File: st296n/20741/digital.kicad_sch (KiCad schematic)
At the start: 61 parts, among them J2 ID, Q14 "1A", U1 8051, U13 74LS155, U2 74LS573, U21 74LS174, U22 74LS174, U23 74LS174, U24 74LS257, U27 74LS00, U28 74LS196, U29 74LS123, U3 74LS14, U30 74F08, U4 CDM6264, U9 11741-502, Y1 10MHz, Y2 20MHz

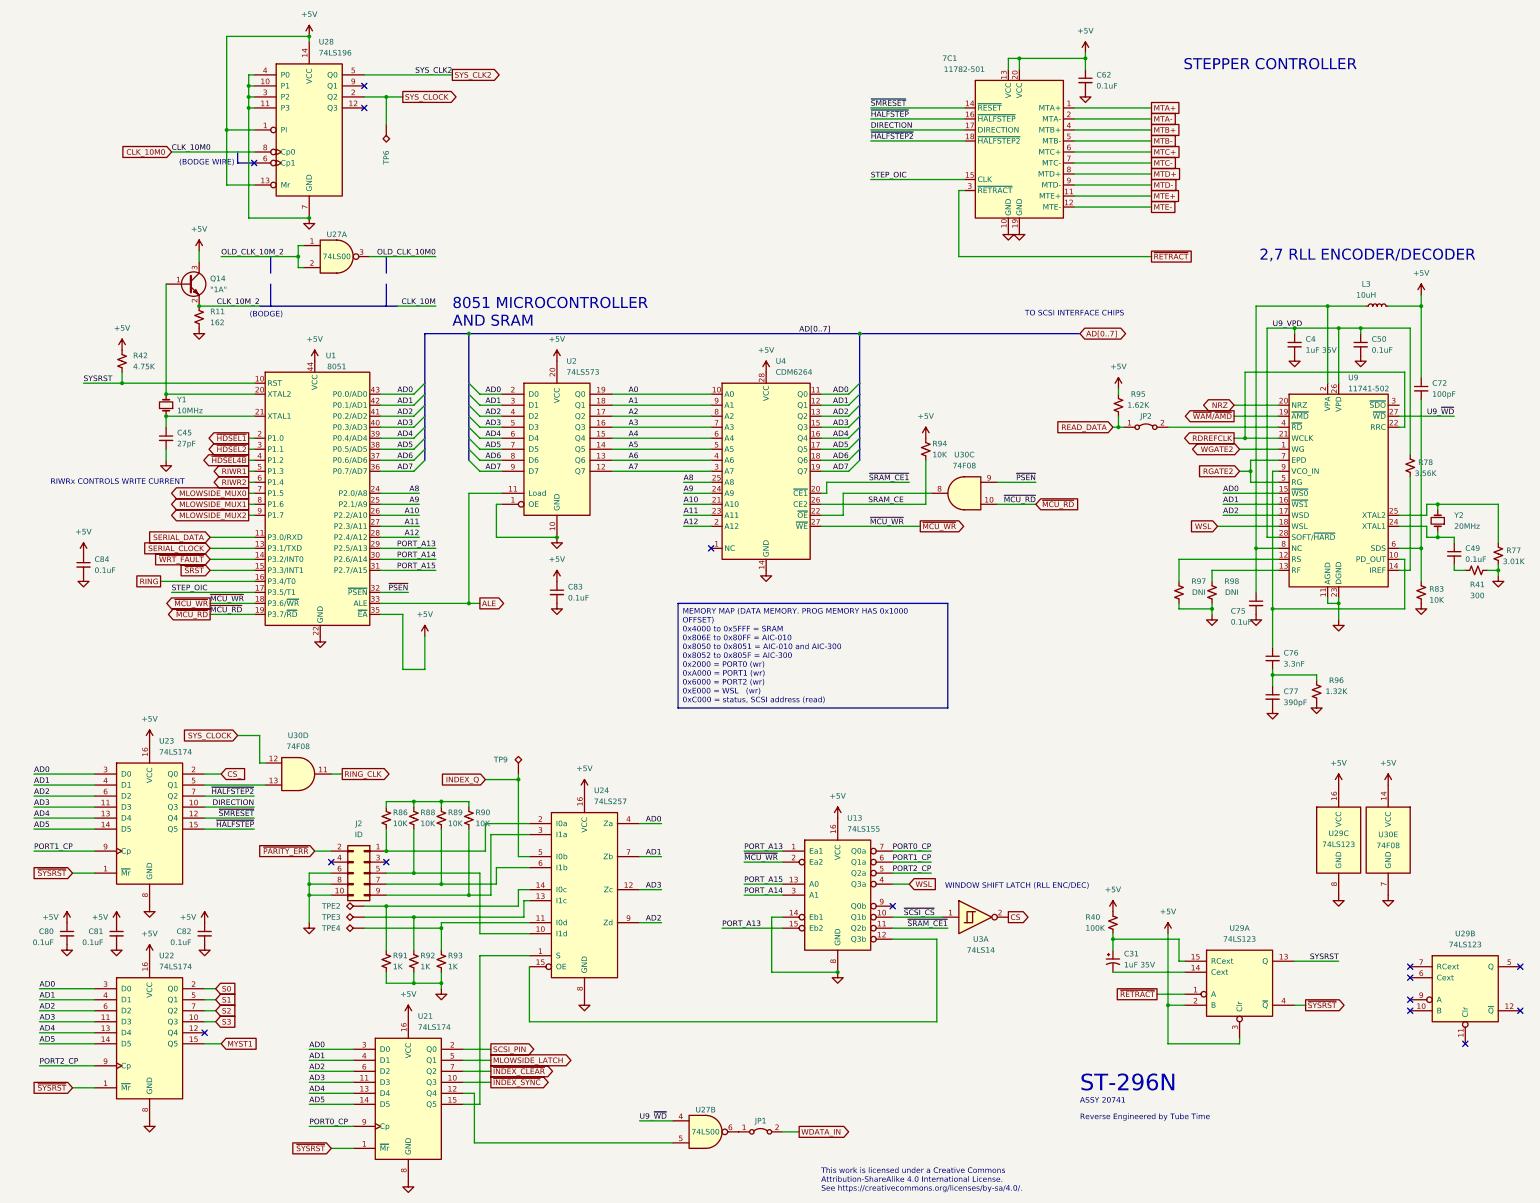
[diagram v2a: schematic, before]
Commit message: Add ST-251N. Update ST-296N to show changes.
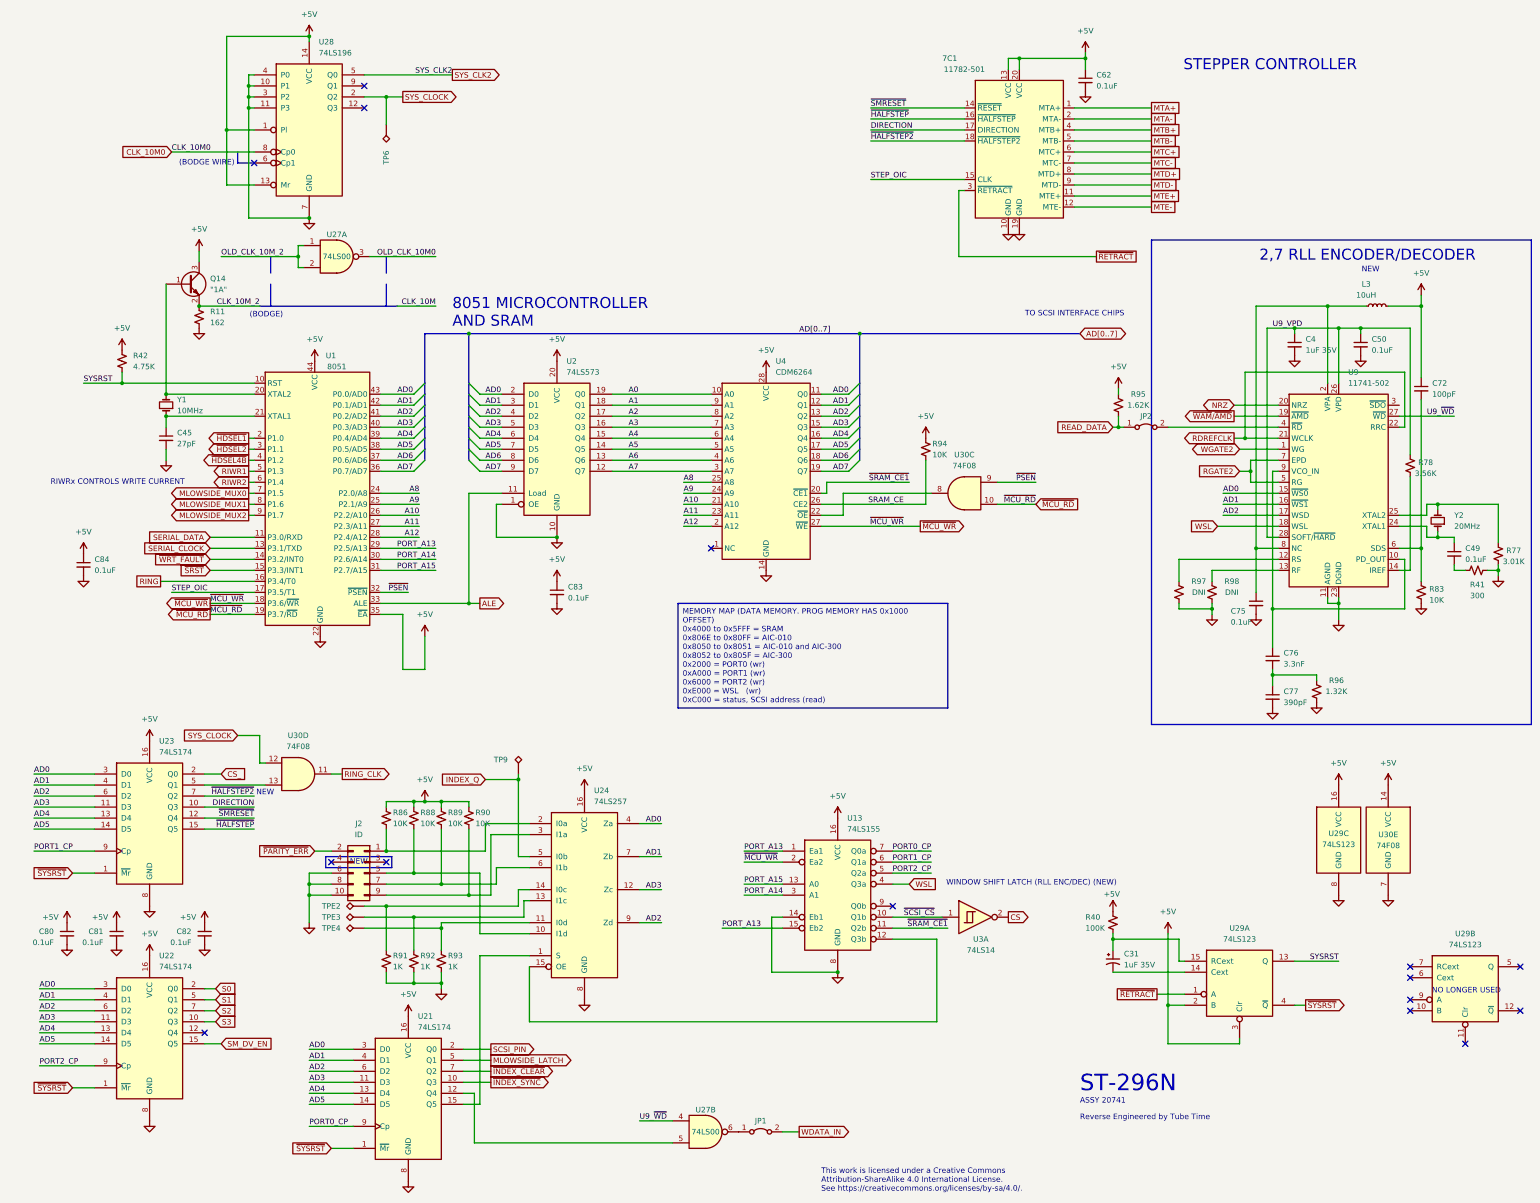
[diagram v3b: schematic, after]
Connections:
- net +5V: now also R86.2, R88.2, R89.2, R90.2
- net MYST1 renamed SM_DV_EN
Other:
- note added: "NEW"
- note added: "NO LONGER USED"
- note added: "WINDOW SHIFT LATCH (RLL ENC/DEC) (NEW)"
- note removed: "WINDOW SHIFT LATCH (RLL ENC/DEC)"
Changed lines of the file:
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@@
 	)
 	(junction
+		(at 151.13 193.04)
+		(diameter 0)
+		(color 0 0 0 0)
+	)
+	(junction
 		(at 351.79 83.82)
 		(diameter 0)
@@
 			(width 0)
 			(type default)
+			(color 255 0 255 1)
 		)
 	)
@@
 			(width 0)
 			(type default)
+			(color 255 0 255 1)
 		)
 	)
@@
 		)
 	)
+	(wire
+		(pts
+			(xy 151.13 193.04) (xy 148.59 193.04)
+		)
+		(stroke
+			(width 0)
+			(type default)
+		)
+	)
 	(bus
 		(pts
@@
 	(wire
 		(pts
-			(xy 274.32 67.31) (xy 318.77 67.31)
+			(xy 274.32 67.31) (xy 306.07 67.31)
 		)
 		(stroke
 			(width 0)
 			(type default)
+			(color 255 0 255 1)
 		)
 	)
@@
 			(width 0)
 			(type default)
+			(color 255 0 255 1)
 		)
 	)
@@
 	(wire
 		(pts
-			(xy 154.94 193.04) (xy 148.59 193.04)
+			(xy 154.94 193.04) (xy 151.13 193.04)
 		)
 		(stroke
@@
 		)
 	)
+	(rectangle
+		(start 318.77 63.5)
+		(end 406.4 175.26)
+		(stroke
+			(width 0)
+			(type default)
+			(color 255 0 255 1)
+		)
+		(fill
+			(type none)
+		)
+	)
+	(rectangle
+		(start 128.27 205.74)
+		(end 143.51 208.28)
+		(stroke
+			(width 0)
+			(type default)
+			(color 255 0 255 1)
+		)
+		(fill
+			(type none)
+		)
+	)
 	(text_box "MEMORY MAP (DATA MEMORY. PROG MEMORY HAS 0x1000 OFFSET)\n0x4000 to 0x5FFF = SRAM\n0x806E to 0x80FF = AIC-010\n0x8050 to 0x8051 = AIC-010 and AIC-300\n0x8052 to 0x805F = AIC-300\n0x2000 = PORT0 (wr)\n0xA000 = PORT1 (wr)\n0x6000 = PORT2 (wr)\n0xE000 = WSL   (wr)\n0xC000 = status, SCSI address (read)\n\n"
 		(exclude_from_sim no)
@@
 		)
 	)
+	(text "NO LONGER USED"
+		(exclude_from_sim no)
+		(at 391.414 236.728 0)
+		(effects
+			(font
+				(size 1.27 1.27)
+				(color 255 0 255 1)
+			)
+		)
+	)
 	(text "2,7 RLL ENCODER/DECODER"
 		(exclude_from_sim no)
@@
 			(font
 				(size 2.54 2.54)
+				(color 255 0 255 1)
 			)
 			(justify left bottom)
@@
 		)
 	)
-	(text "WINDOW SHIFT LATCH (RLL ENC/DEC)"
+	(text "WINDOW SHIFT LATCH (RLL ENC/DEC) (NEW)"
+		(exclude_from_sim no)
+		(at 291.084 211.836 0)
+		(effects
+			(font
+				(size 1.27 1.27)
+				(color 255 0 255 1)
+			)
+		)
+	)
+	(text "NEW"
 		(exclude_from_sim no)
-		(at 287.782 212.598 0)
+		(at 369.316 70.358 0)
 		(effects
 			(font
 				(size 1.27 1.27)
+				(color 255 0 255 1)
 			)
 		)
@@
 		)
 	)
+	(text "NEW"
+		(exclude_from_sim no)
+		(at 135.89 207.01 0)
+		(effects
+			(font
+				(size 1.27 1.27)
+				(color 255 0 255 1)
+			)
+		)
+	)
 	(text "RIWRx CONTROLS WRITE CURRENT"
 		(exclude_from_sim no)
@@
 		)
 	)
+	(text "NEW"
+		(exclude_from_sim no)
+		(at 114.3 191.008 0)
+		(effects
+			(font
+				(size 1.27 1.27)
+				(color 255 0 255 1)
+			)
+		)
+	)
 	(label "A6"
 		(at 198.12 114.3 0)
@@
 			(font
 				(size 1.27 1.27)
+				(color 255 0 255 1)
 			)
 			(justify left bottom)
@@
 			(font
 				(size 1.27 1.27)
+				(color 255 0 255 1)
 			)
 			(justify right bottom)
@@
 		)
 	)
-	(global_label "MYST1"
+	(global_label "SM_DV_EN"
 		(shape input)
 		(at 104.14 248.92 0)
@@
 		)
 		(property "Intersheetrefs" "${INTERSHEET_REFS}"
-			(at 113.0518 248.92 0)
+			(at 116.5594 248.92 0)
 			(effects
 				(font
@@
 	(global_label "~{RETRACT}"
 		(shape passive)
-		(at 318.77 67.31 0)
+		(at 306.07 67.31 0)
 		(fields_autoplaced yes)
 		(effects
@@
 		)
 		(property "Intersheetrefs" "${INTERSHEET_REFS}"
-			(at 328.6267 67.31 0)
+			(at 315.9267 67.31 0)
 			(effects
 				(font
@@
 		(on_board yes)
 		(dnp no)
-		(fields_autoplaced yes)
 		(property "Reference" "#PWR0136"
 			(at 309.88 222.25 0)
@@
 		)
 		(property "Value" "+5V"
-			(at 309.88 213.36 0)
+			(at 309.626 214.376 0)
 			(effects
 				(font
@@
 	)
 	(symbol
+		(lib_id "power:+5V")
+		(at 151.13 193.04 0)
+		(unit 1)
+		(exclude_from_sim no)
+		(in_bom yes)
+		(on_board yes)
+		(dnp no)
+		(fields_autoplaced yes)
+		(property "Reference" "#PWR0159"
+			(at 151.13 196.85 0)
+			(effects
+				(font
+					(size 1.27 1.27)
+				)
+				(hide yes)
+			)
+		)
+		(property "Value" "+5V"
+			(at 151.13 187.96 0)
+			(effects
+				(font
+					(size 1.27 1.27)
+				)
+			)
+		)
+		(property "Footprint" ""
+			(at 151.13 193.04 0)
+			(effects
+				(font
+					(size 1.27 1.27)
+				)
+				(hide yes)
+			)
+		)
+		(property "Datasheet" ""
+			(at 151.13 193.04 0)
+			(effects
+				(font
+					(size 1.27 1.27)
+				)
+				(hide yes)
+			)
+		)
+		(property "Description" ""
+			(at 151.13 193.04 0)
+			(effects
+				(font
+					(size 1.27 1.27)
+				)
+				(hide yes)
+			)
+		)
+		(pin "1"
+		)
+		(instances
+			(project "st296n_20741"
+				(path "/f29784b7-b8b8-488c-8543-989c9e3b7621/6eebd973-f5b1-4c2e-8b65-8af8189537eb"
+					(reference "#PWR0159")
+					(unit 1)
+				)
+			)
+		)
+	)
+	(symbol
 		(lib_id "power:GND")
 		(at 246.38 232.41 0)
@@
 		(fields_autoplaced yes)
 		(property "Reference" "U9"
-			(at 364.1441 95.25 0)
+			(at 364.1441 93.98 0)
 			(effects
 				(font
@@
 		)
 		(property "Value" "11741-502"
-			(at 364.1441 97.79 0)
+			(at 364.1441 96.52 0)
 			(effects
 				(font
 					(size 1.27 1.27)
+					(color 255 0 255 1)
 				)
 				(justify left)
@@
 				(font
 					(size 1.27 1.27)
+					(color 255 0 255 1)
 				)
 			)
@@
 				(font
 					(size 1.27 1.27)
+					(color 255 0 255 1)
 				)
 				(justify right)
